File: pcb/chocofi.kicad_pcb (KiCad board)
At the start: 2 copper layers, 111.3 x 90 mm, 55 parts, among them J1 MJ-4PP-9, J2 OLED, SW10 SW_PUSH, SW11 SW_PUSH, SW12 SW_PUSH, SW14 SW_PUSH, SW15 SW_PUSH, SW16 SW_PUSH, SW17 SW_PUSH, SW18 SW_PUSH, SW19 SW_PUSH, SW2 SW_PUSH, SW20 SW_PUSH, SW21 SW_PUSH, SW3 SW_PUSH, SW4 SW_PUSH, SW5 SW_PUSH, SW6 SW_PUSH, SW8 SW_PUSH, SW9 SW_PUSH, U1 ProMicro

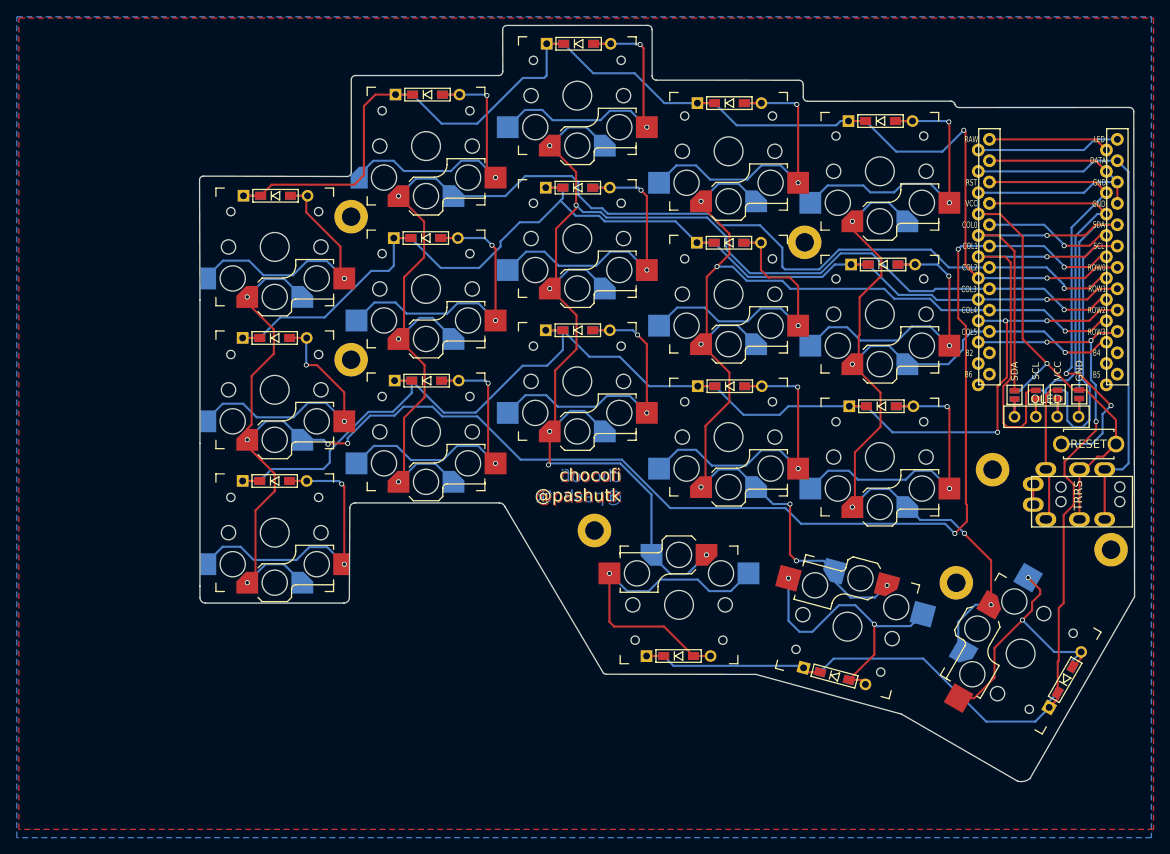
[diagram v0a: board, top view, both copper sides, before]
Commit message: Enlarged hole for trackpoint
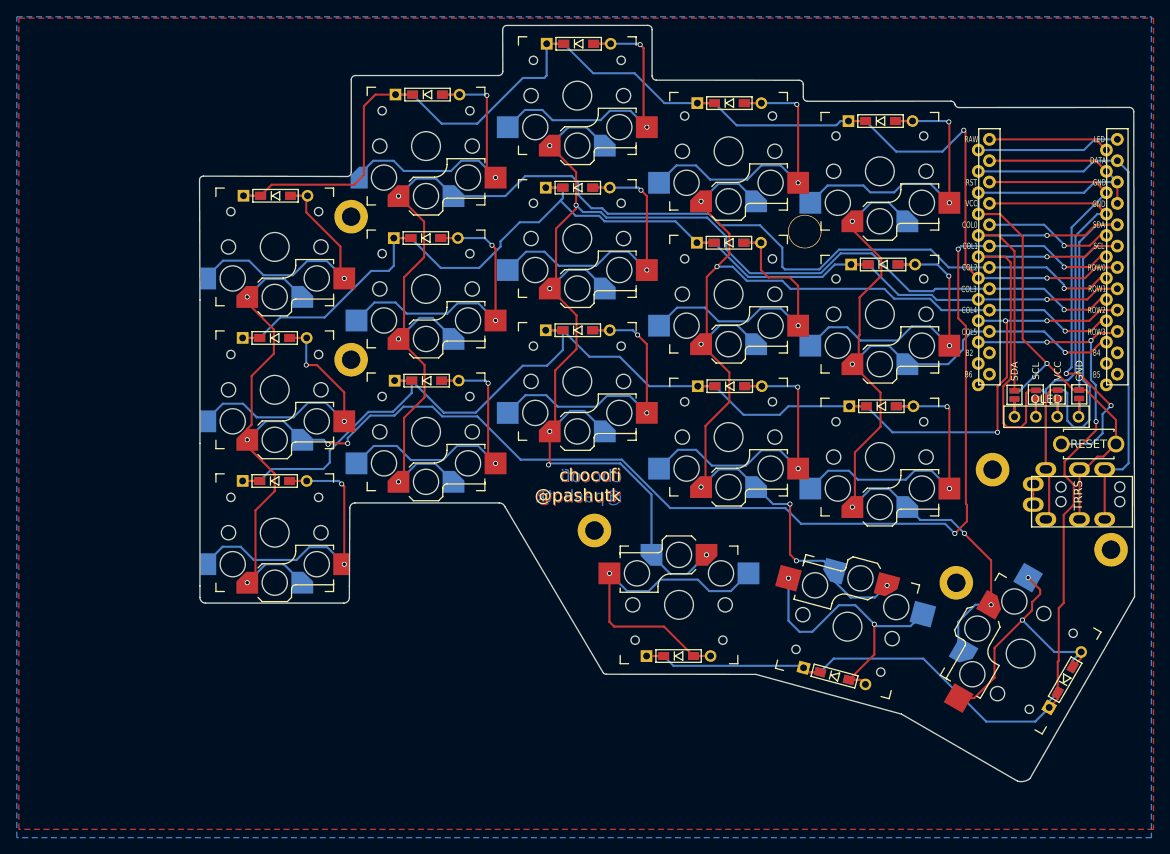
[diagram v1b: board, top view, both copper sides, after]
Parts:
- moved h7 1.27 mm to (149.0, 68.6)
